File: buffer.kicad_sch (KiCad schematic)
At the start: 5 parts, among them J12 BUF_EN, U6 BUF602ID

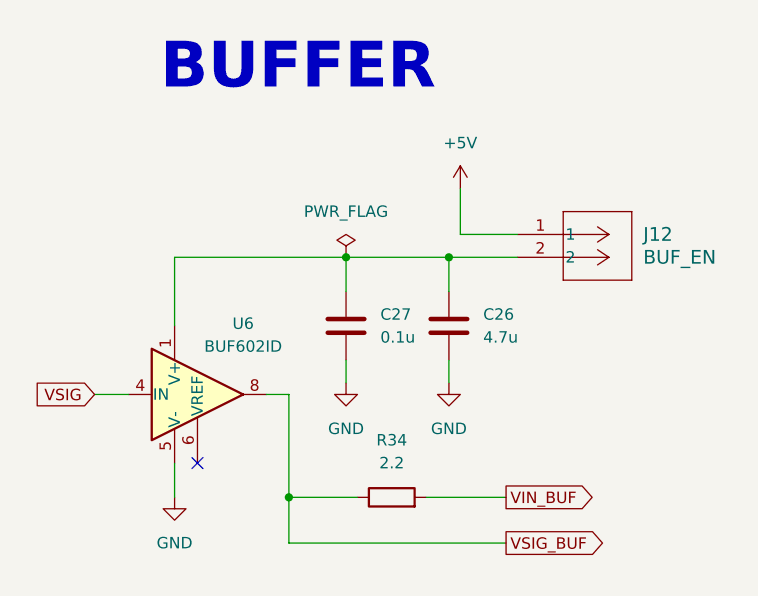
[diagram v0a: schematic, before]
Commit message: Schematic freeze: add C10, probe headers, buffer link and Teensy taps
SCHEMATIC FROZEN at this commit. 164 parts, 108 nets, ERC 0 errors.
All remaining work is layout. Do not change the schematic without
telling the group.

Top sheet:
- C10 (10u) back between VOUT_LDO and the J6 SMA
- J18 VIN_PROBE, J19 VREF_PROBE, J20 VOUT_PROBE: 2-pin headers with
  pin 1 on VDD_LDO, NR, VOUT_LDO and pin 2 on GND
- IBIAS and NR labels changed from local to global

Buffer sheet:
- R40 (0 ohm) in series between R34 and VDD_LDO

MCU sheet:
- J21 to J25, VG0_PROBE to VG4_PROBE: 2-pin headers with pin 1 on
  VG0 to VG4 and pin 2 on GND
- R51, R52, R53 (0 ohm, DNP) from Teensy pins 23, 22, 21 to MD,
  IBIAS, NR
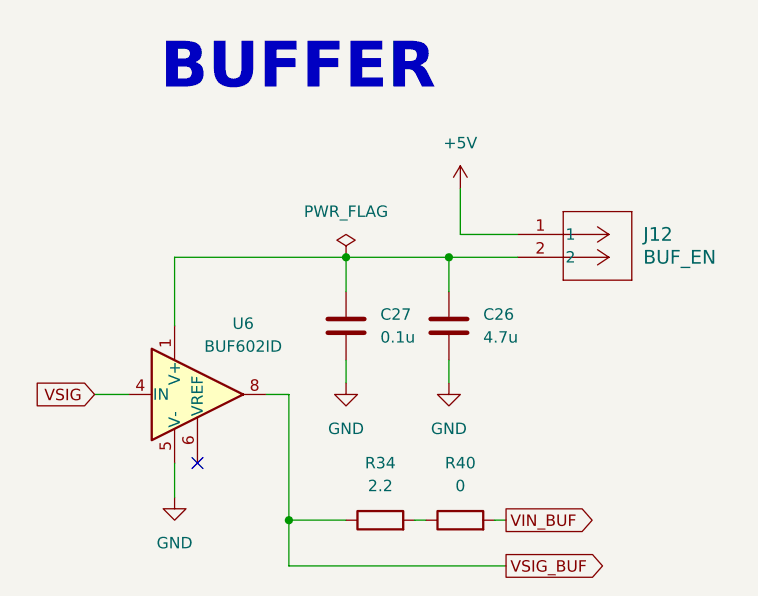
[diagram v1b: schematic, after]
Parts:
- added R40: 0, Resistor_SMD:R_0603_1608Metric_Pad0.98x0.95mm_HandSolder, symbol Device:R
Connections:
- net VIN_BUF: now also R40.2; no longer R34.2
- new net: R34.2, R40.1
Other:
- moved on the sheet: R34
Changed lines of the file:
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@@
 	)
 	(junction
-		(at 49.53 78.74)
+		(at 49.53 81.28)
 		(diameter 0)
 		(color 0 0 0 0)
@@
 	(wire
 		(pts
+			(xy 46.99 67.31) (xy 49.53 67.31)
+		)
+		(stroke
+			(width 0)
+			(type default)
+		)
+	)
+	(wire
+		(pts
 			(xy 67.31 63.5) (xy 67.31 66.04)
 		)
@@
 	(wire
 		(pts
-			(xy 49.53 67.31) (xy 49.53 83.82)
-		)
-		(stroke
-			(width 0)
-			(type default)
-		)
-	)
-	(wire
-		(pts
-			(xy 46.99 67.31) (xy 49.53 67.31)
+			(xy 49.53 67.31) (xy 49.53 86.36)
 		)
 		(stroke
@@
 	(wire
 		(pts
-			(xy 49.53 83.82) (xy 73.66 83.82)
+			(xy 49.53 86.36) (xy 73.66 86.36)
 		)
 		(stroke
@@
 	(wire
 		(pts
-			(xy 64.77 78.74) (xy 73.66 78.74)
-		)
-		(stroke
-			(width 0)
-			(type default)
-		)
-	)
-	(wire
-		(pts
-			(xy 49.53 78.74) (xy 57.15 78.74)
+			(xy 63.5 81.28) (xy 64.77 81.28)
+		)
+		(stroke
+			(width 0)
+			(type default)
+		)
+	)
+	(wire
+		(pts
+			(xy 49.53 81.28) (xy 55.88 81.28)
+		)
+		(stroke
+			(width 0)
+			(type default)
+		)
+	)
+	(wire
+		(pts
+			(xy 72.39 81.28) (xy 73.66 81.28)
 		)
 		(stroke
@@
 	(global_label "VIN_BUF"
 		(shape output)
-		(at 73.66 78.74 0)
+		(at 73.66 81.28 0)
 		(fields_autoplaced yes)
 		(effects
@@
 		)
 		(property "Intersheetrefs" "${INTERSHEET_REFS}"
-			(at 84.3258 78.74 0)
+			(at 84.3258 81.28 0)
 			(hide yes)
 			(show_name no)
@@
 	(global_label "VSIG_BUF"
 		(shape output)
-		(at 73.66 83.82 0)
+		(at 73.66 86.36 0)
 		(fields_autoplaced yes)
 		(effects
@@
 		)
 		(property "Intersheetrefs" "${INTERSHEET_REFS}"
-			(at 85.4748 83.82 0)
+			(at 85.4748 86.36 0)
 			(hide yes)
 			(show_name no)
@@
 	(symbol
 		(lib_id "Device:R")
-		(at 60.96 78.74 90)
+		(at 68.58 81.28 90)
+		(unit 1)
+		(body_style 1)
+		(exclude_from_sim no)
+		(in_bom yes)
+		(on_board yes)
+		(in_pos_files yes)
+		(dnp no)
+		(fields_autoplaced yes)
+		(property "Reference" "R40"
+			(at 68.58 74.93 90)
+			(show_name no)
+			(do_not_autoplace no)
+			(effects
+				(font
+					(size 1.27 1.27)
+				)
+			)
+		)
+		(property "Value" "0"
+			(at 68.58 77.47 90)
+			(show_name no)
+			(do_not_autoplace no)
+			(effects
+				(font
+					(size 1.27 1.27)
+				)
+			)
+		)
+		(property "Footprint" "Resistor_SMD:R_0603_1608Metric_Pad0.98x0.95mm_HandSolder"
+			(at 68.58 83.058 90)
+			(hide yes)
+			(show_name no)
+			(do_not_autoplace no)
+			(effects
+				(font
+					(size 1.27 1.27)
+				)
+			)
+		)
+		(property "Datasheet" "https://www.vishay.com/docs/20043/crcwhpe3.pdf"
+			(at 68.58 81.28 0)
+			(hide yes)
+			(show_name no)
+			(do_not_autoplace no)
+			(effects
+				(font
+					(size 1.27 1.27)
+				)
+			)
+		)
+		(property "Description" "RES 0 OHM JUMPER 1/3W 0603"
+			(at 68.58 81.28 0)
+			(hide yes)
+			(show_name no)
+			(do_not_autoplace no)
+			(effects
+				(font
+					(size 1.27 1.27)
+				)
+			)
+		)
+		(property "Distributer Link 1" "https://www.digikey.com/en/products/detail/vishay-dale/CRCW06030000Z0EAHP/2222231"
+			(at 68.58 81.28 0)
+			(hide yes)
+			(show_name no)
+			(do_not_autoplace no)
+			(effects
+				(font
+					(size 1.27 1.27)
+				)
+			)
+		)
+		(property "Manufacturer Part Number" "CRCW06030000Z0EAHP"
+			(at 68.58 81.28 0)
+			(hide yes)
+			(show_name no)
+			(do_not_autoplace no)
+			(effects
+				(font
+					(size 1.27 1.27)
+				)
+			)
+		)
+		(property "Manufacturer" "Vishay Dale"
+			(at 68.58 81.28 0)
+			(hide yes)
+			(show_name no)
+			(do_not_autoplace no)
+			(effects
+				(font
+					(size 1.27 1.27)
+				)
+			)
+		)
+		(pin "1"
+		)
+		(pin "2"
+		)
+		(instances
+			(project "ldo_bringup_board_ee372"
+				(path "/d41ff68c-d87d-4b82-b500-4ee675d17cf6/1c4e65a0-f492-4ef9-b030-c6464e799e64"
+					(reference "R40")
+					(unit 1)
+				)
+			)
+		)
+	)
+	(symbol
+		(lib_id "Device:R")
+		(at 59.69 81.28 90)
 		(unit 1)
 		(body_style 1)
@@
 		(fields_autoplaced yes)
 		(property "Reference" "R34"
-			(at 60.96 72.39 90)
+			(at 59.69 74.93 90)
 			(show_name no)
 			(do_not_autoplace no)
@@
 		)
 		(property "Value" "2.2"
-			(at 60.96 74.93 90)
+			(at 59.69 77.47 90)
 			(show_name no)
 			(do_not_autoplace no)
@@
 		)
 		(property "Footprint" "Resistor_SMD:R_0603_1608Metric_Pad0.98x0.95mm_HandSolder"
-			(at 60.96 80.518 90)
+			(at 59.69 83.058 90)
 			(hide yes)
 			(show_name no)
@@
 		)
 		(property "Datasheet" "https://industrial.panasonic.com/cdbs/www-data/pdf/RDN0000/AOA0000C313.pdf"
-			(at 60.96 78.74 0)
+			(at 59.69 81.28 0)
 			(hide yes)
 			(show_name no)
@@
 		)
 		(property "Description" "RES 2.2 OHM 1% 1/10W 0603"
-			(at 60.96 78.74 0)
+			(at 59.69 81.28 0)
 			(hide yes)
 			(show_name no)
@@
 		)
 		(property "Manufacturer" "Panasonic Industry"
-			(at 60.96 78.74 0)
+			(at 59.69 81.28 0)
 			(hide yes)
 			(show_name no)
@@
 		)
 		(property "Manufacturer Part Number" "ERJ-3RQF2R2V"
-			(at 60.96 78.74 0)
+			(at 59.69 81.28 0)
 			(hide yes)
 			(show_name no)
@@
 		)
 		(property "Distributer Link 1" "https://www.digikey.com/en/products/detail/panasonic-industry/ERJ-3RQF2R2V/308066"
-			(at 60.96 78.74 0)
-			(hide yes)
-			(show_name no)
+			(at 59.69 81.28 0)
+			(hide yes)
+			(show_name no)

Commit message: Add bring-up notes to the schematic
Text notes only, no parts or nets change. Leave R3, R21, R29 to R32,
R40, R44 and R55 off at first. Possibly lift C6 and C11 when driving
VIN from the buffer. Add a large pull-down on the buffer input.
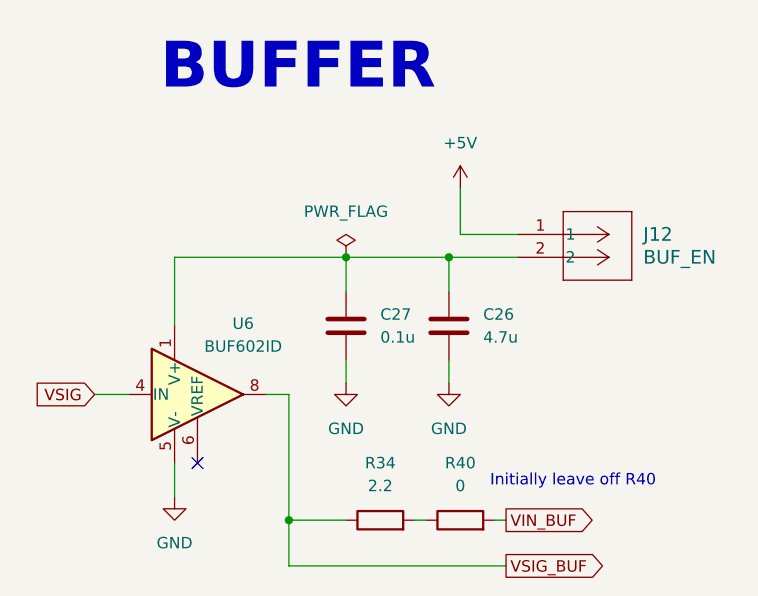
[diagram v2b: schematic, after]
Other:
- note added: "Initially leave off R40"
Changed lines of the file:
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@@
 		(comment 4 "Caleb Ketchum")
+	)
+	(text "Initially leave off R40"
+		(exclude_from_sim yes)
+		(at 71.882 76.962 0)
+		(effects
+			(font
+				(size 1.27 1.27)
+			)
+			(justify left)
+		)
 	)
 	(text "BUFFER"
